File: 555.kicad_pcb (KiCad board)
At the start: 2 copper layers, 50 x 50 mm, 7 parts, among them U1 DIP-8_W7.62mm

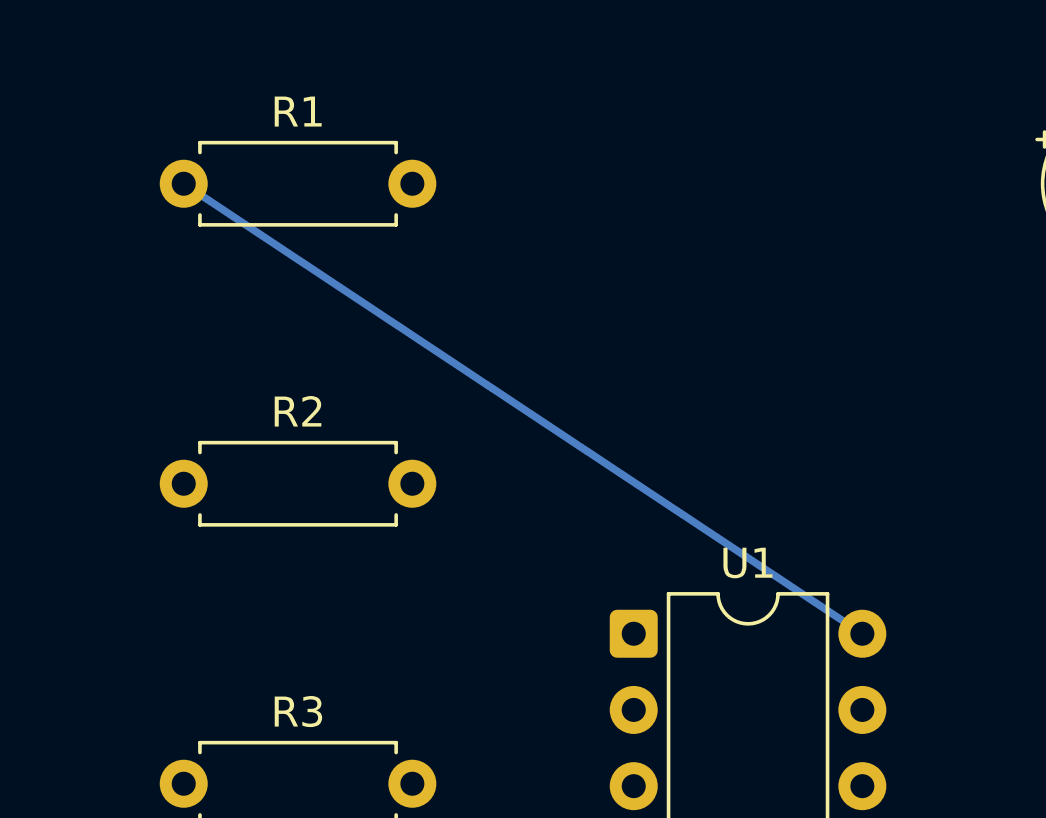
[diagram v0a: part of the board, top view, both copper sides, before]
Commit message: Fix CI failure and address code review feedback
- Fixed 'pip: not found' in GitHub Actions by using 'python3 -m pip'.
- Corrected KiCad file format version and generator version in artifacts.
- Renamed documentation files to match required typos: DECISION_LOG.md and FAILED_ATTEMPTS.md.
- Corrected LED polarity in PCB generation script.
- Cleaned up temporary logs and ERC/DRC reports from repository.
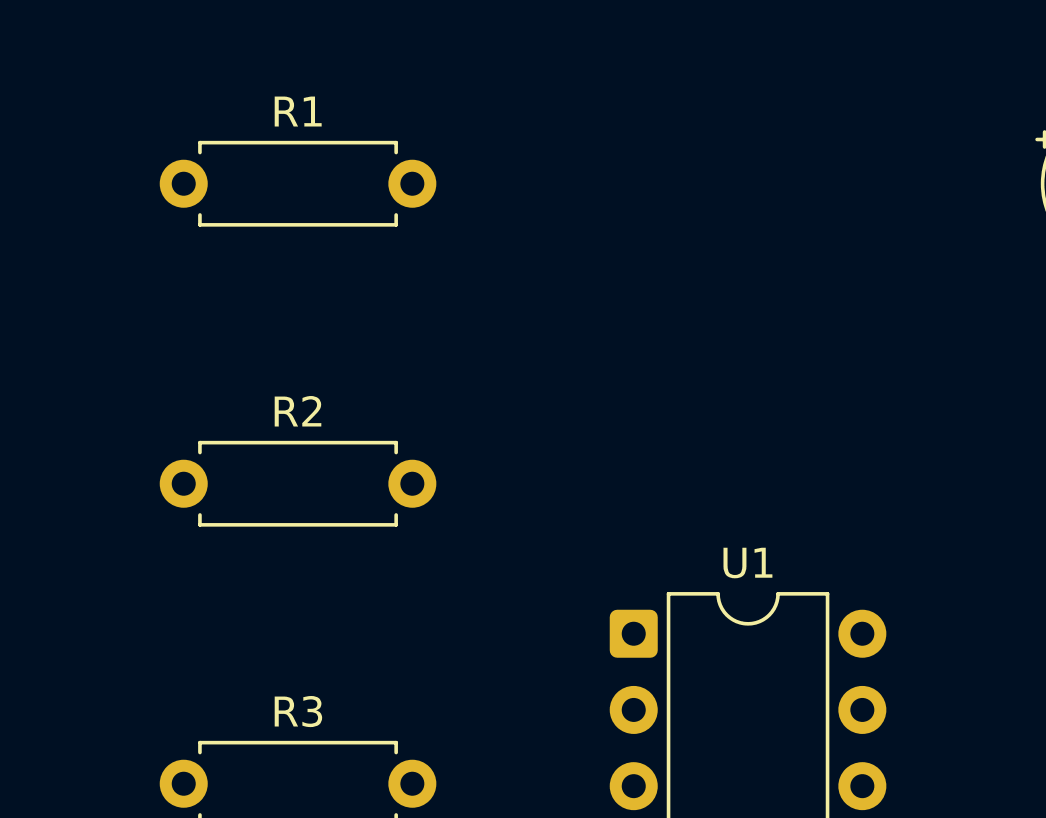
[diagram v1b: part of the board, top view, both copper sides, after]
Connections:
- D1 pad 1: OUT -> OUT_LED
- D1 pad 2: OUT_LED -> OUT
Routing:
- net VCC: track 27.1 -> 0.00 mm
